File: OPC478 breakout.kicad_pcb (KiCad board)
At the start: 2 copper layers, 33 x 30.5 mm, 16 parts, among them J1 Conn_01x05_Pin, J2 AudioPlug4, J3 Conn_01x01_Socket, J4 Conn_01x01_Socket, Q1 BC557, Q2 BC547

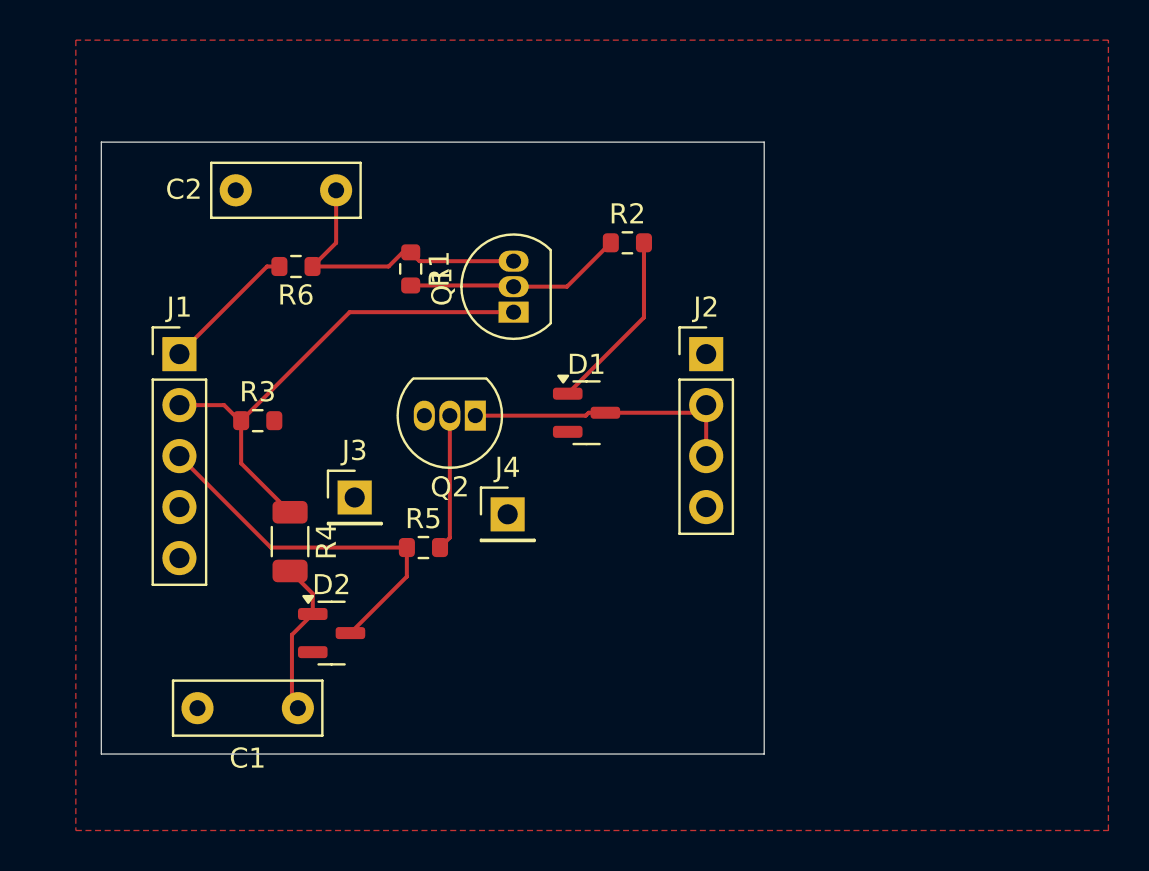
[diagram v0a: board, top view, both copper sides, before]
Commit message: compacted and simplified layout, widened traces, first viable board produced
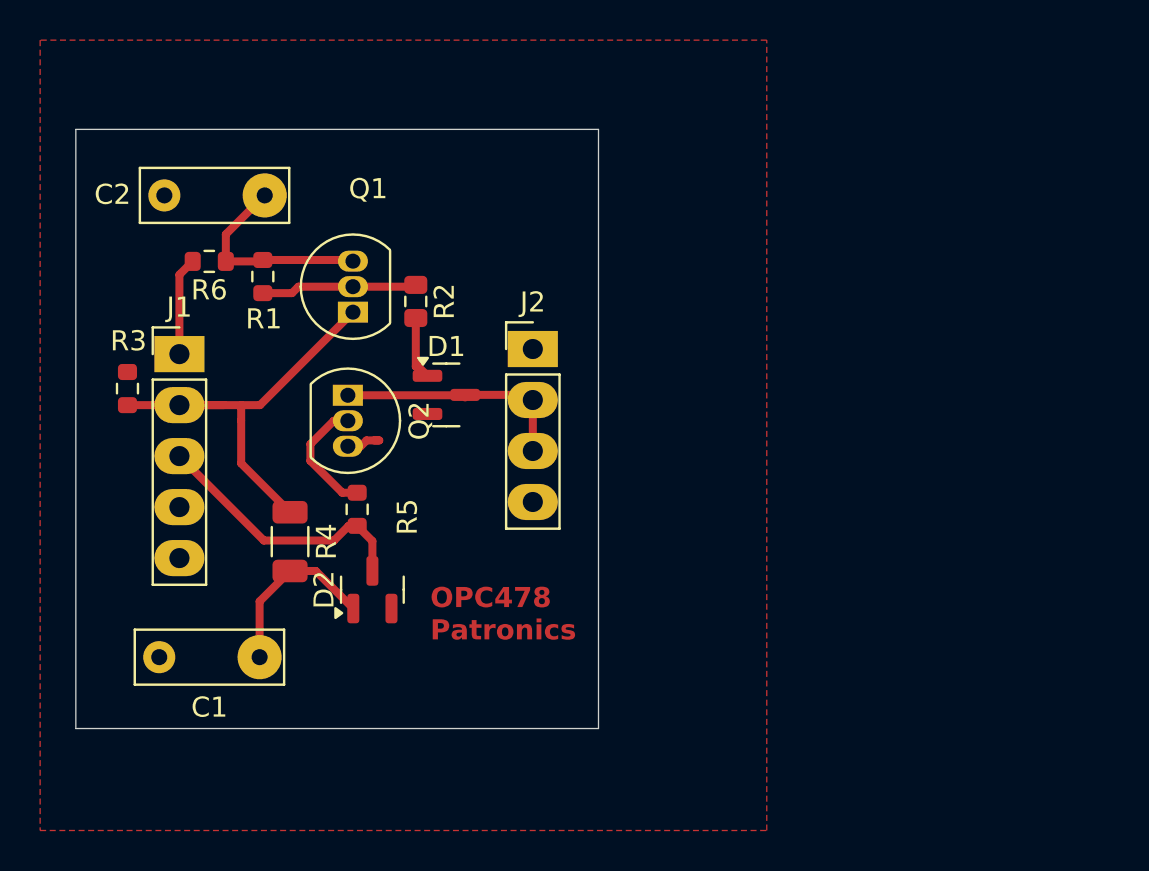
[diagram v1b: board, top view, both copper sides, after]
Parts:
- removed J3, J4: Conn_01x01_Socket, Connector_PinHeader_2.54mm:PinHeader_1x01_P2.54mm_Vertical
- moved R2 10.9 mm to (116.0, 76.5), turned to -90 degrees
- moved J2 8.64 mm to (121.8, 78.9)
- moved Q1 8.00 mm to (112.9, 77.0)
- moved R1 7.38 mm to (108.4, 75.3)
- moved D1 7.04 mm to (117.5, 81.2)
- moved R3 6.68 mm to (101.6, 80.9), turned to 90 degrees
- moved Q2 6.43 mm to (112.6, 81.2), turned to -90 degrees
- moved R6 4.33 mm to (105.7, 74.5)
- moved R5 3.81 mm to (113.1, 86.9), turned to 90 degrees
- moved C2 3.57 mm to (108.5, 71.2)
- moved C1 3.18 mm to (108.2, 94.2)
- moved D2 2.96 mm to (113.8, 90.9), turned to 90 degrees
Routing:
- net Net-(D1-A): track 9.09 -> 3.20 mm
- net Net-(D2-K): track 18.6 -> 13.5 mm
- net Net-(Q1-E): track 14.8 -> 10.5 mm
- net Net-(Q1-B): track 10.9 -> 7.79 mm
- net Net-(J1-Pin_2): track 24.8 -> 21.7 mm
- net Net-(D1-K): track 14.3 -> 11.9 mm
- net GND: track 0.00 -> 1.94 mm
- net Net-(J1-Pin_1): track 6.79 -> 4.89 mm
- net Net-(D2-A): track 7.85 -> 8.85 mm
- net Net-(Q2-B): track 6.77 -> 6.17 mm
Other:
- board size 33 x 30.5 mm -> 26 x 29.8 mm
- board text added: "OPC478 Patronics"
